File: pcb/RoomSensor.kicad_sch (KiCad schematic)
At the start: 38 parts, among them J1 FH34SRJ-24S-0.5SH50, J2 USB_C_Receptacle_PowerOnly_6P, J3 programming, Q1 SI1308EDL-T1-GE3, SW1 SW_Push, U1 ESP32-WROOM-32D

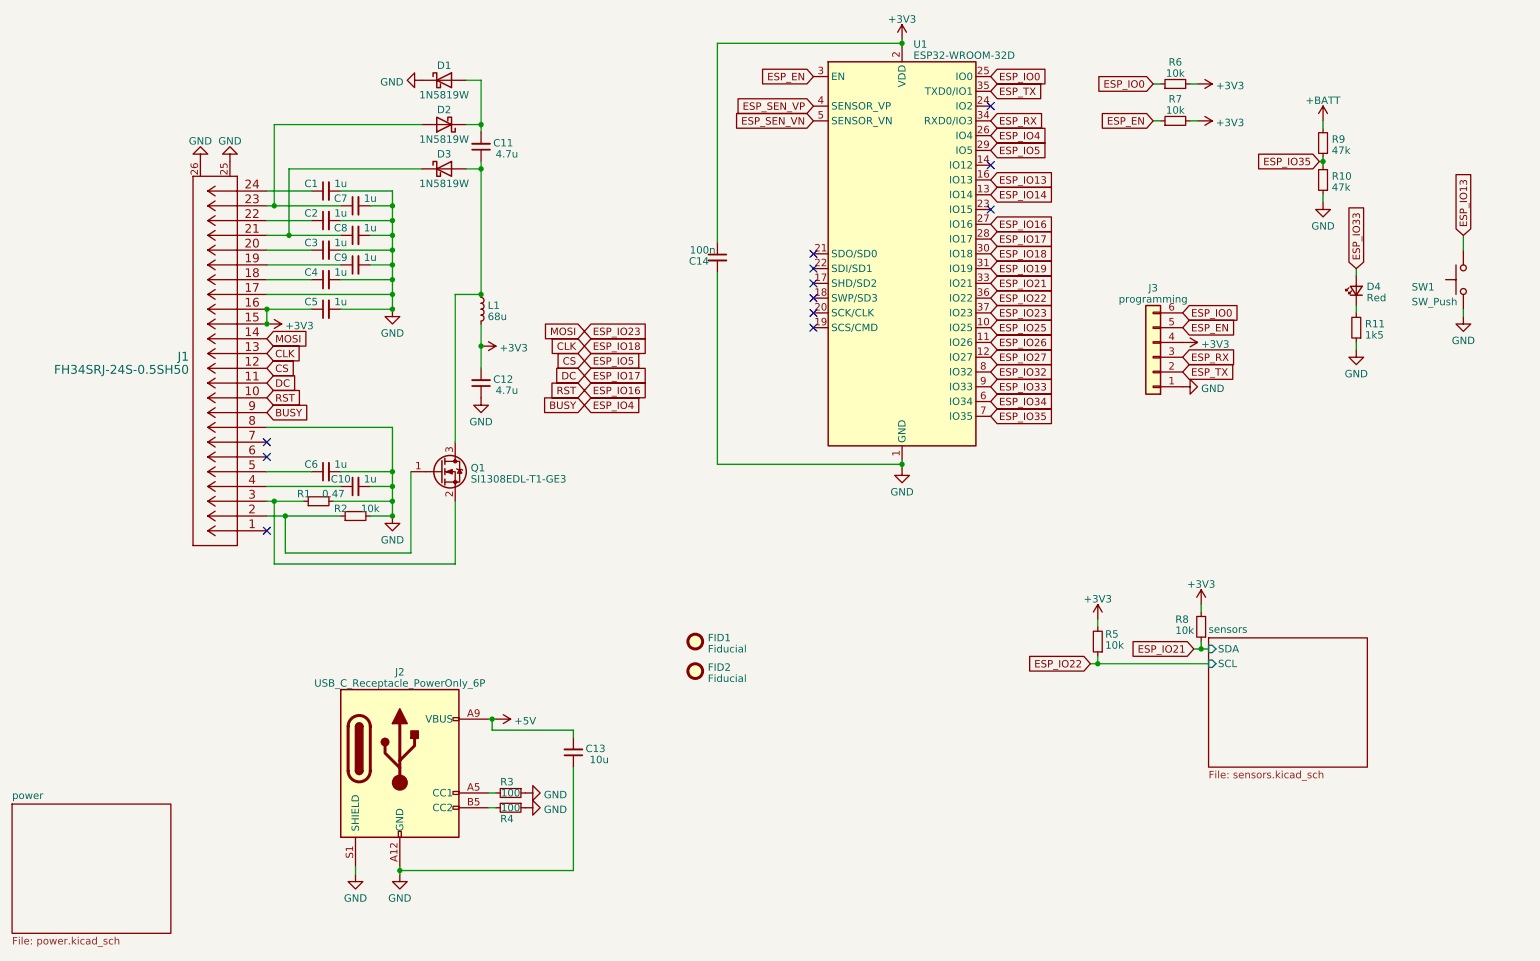
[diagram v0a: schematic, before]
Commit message: Increase PCB size and fix EPD pinout
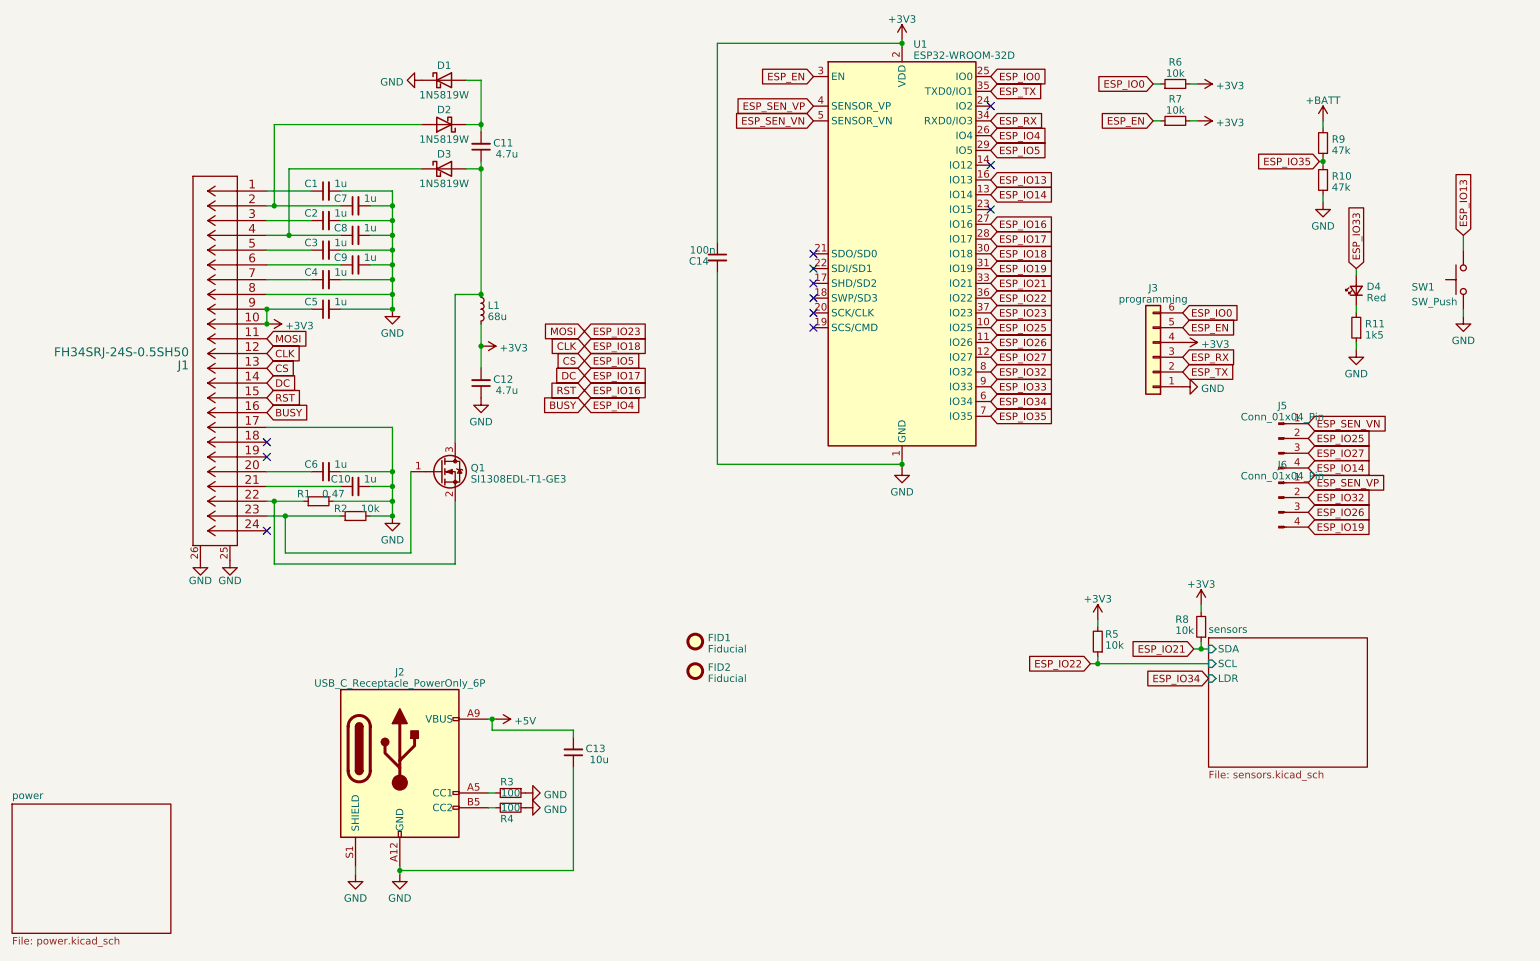
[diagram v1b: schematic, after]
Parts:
- added J5, J6: Conn_01x04_Pin, Connector_PinHeader_2.54mm:PinHeader_1x04_P2.54mm_Vertical, symbol Connector:Conn_01x04_Pin
- FID2: footprint Fiducial:Fiducial_0.5mm_Mask1mm -> Fiducial:Fiducial_0.5mm_Mask1.5mm
- J2: footprint Custom:TYPE-C-31-M-17_B -> Custom:TYPE-C 6P LCH10.0
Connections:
- net +3V3: now also J1.10, J1.9; no longer J1.15, J1.16
- net BUSY: now also J1.16; no longer J1.9
- net CLK: now also J1.12; no longer J1.13
- net CS: now also J1.13; no longer J1.12
- net DC: now also J1.14; no longer J1.11
- net ESP_IO14: now also J5.4 (Pin_4)
- net ESP_IO16: now also J1.15; no longer J1.10
- net ESP_IO19: now also J6.4 (Pin_4)
- net ESP_IO23: now also J1.11; no longer J1.14
- net ESP_IO25: now also J5.2 (Pin_2)
- net ESP_IO26: now also J6.3 (Pin_3)
- net ESP_IO27: now also J5.3 (Pin_3)
- net ESP_IO32: now also J6.2 (Pin_2)
- net ESP_SEN_VN: now also J5.1 (Pin_1)
- net ESP_SEN_VP: now also J6.1 (Pin_1)
- net at C4.1: now also J1.7; no longer J1.18
- net at C8.1, D3.1 (K): now also J1.4; no longer J1.21
- net at C3.1: now also J1.5; no longer J1.20
- net at Q1.2 (S), R1.1: now also J1.22; no longer J1.3
- net at Q1.1 (G), R2.1: now also J1.23; no longer J1.2
- net at C7.1, D2.2 (A): now also J1.2; no longer J1.23
- net at C2.1: now also J1.3; no longer J1.22
- net at J1.1: now also C1.1
- net at J1.19: no longer C9.1
- net at J1.24: no longer C1.1
- net at C10.1: now also J1.21; no longer J1.4
- net at C6.1: now also J1.20; no longer J1.5
- net at J1.6: now also C9.1
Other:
- sheet sensors ports: added LDR; removed none
- moved on the sheet: J1

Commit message: Fix low power issues
- Fix spurious EPD wakeups by adding pull-up to EPD reset line
- Reduce power consumption by switching sensors off with mosfet
- Connect button to reset to reduce power by not needing rtc gpio
- Add solder jumper for silent boot
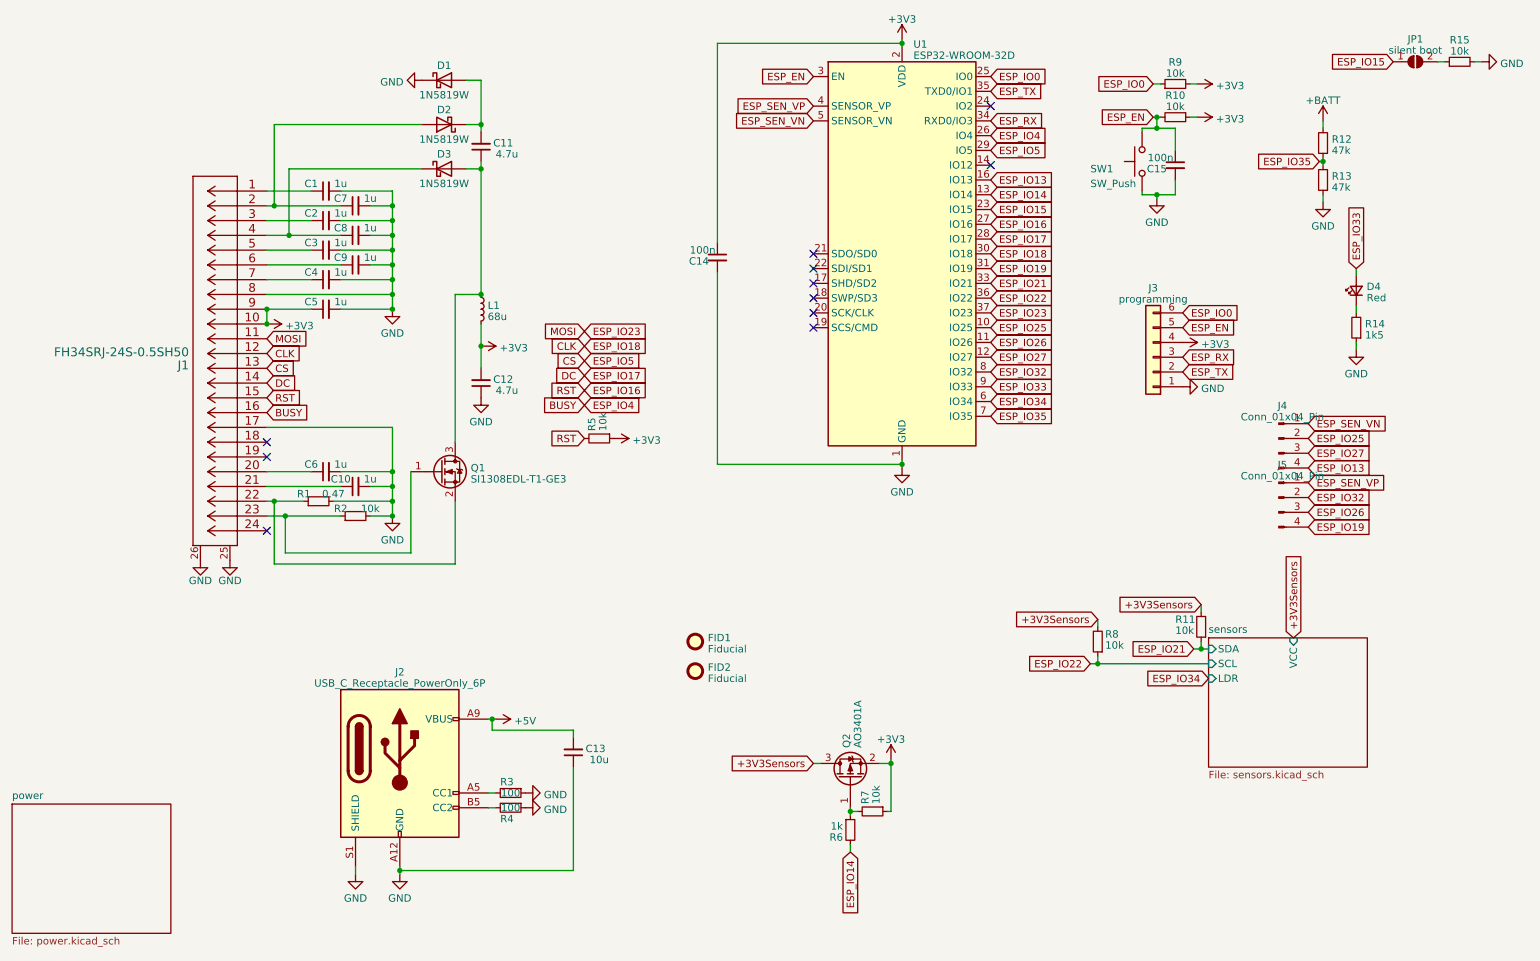
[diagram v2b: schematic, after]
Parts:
- added C15: 100n, Capacitor_SMD:C_0603_1608Metric, symbol Device:C_Small
- added JP1: silent boot, Jumper:SolderJumper-2_P1.3mm_Open_TrianglePad1.0x1.5mm, symbol Jumper:SolderJumper_2_Open
- added Q2: AO3401A, Package_TO_SOT_SMD:SOT-23, symbol Transistor_FET:AO3401A
- added R15, R5, R7: 10k, Resistor_SMD:R_0603_1608Metric, symbol Device:R_Small
- added R6: 1k, Resistor_SMD:R_0603_1608Metric, symbol Device:R_Small
- FID1: footprint Fiducial:Fiducial_0.5mm_Mask1mm -> Fiducial:Fiducial_0.5mm_Mask1.5mm
- renumbered J5 to J4, J6 to J5, R7 to R10, R8 to R11, R9 to R12, R10 to R13, R11 to R14, R5 to R8, R6 to R9
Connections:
- net +3V3: now also R10.1, Q2.2 (S), R5.1, R7.1; no longer R10.2, R11.2, R8.2
- net ESP_EN: now also R10.2, SW1.2, C15.1; no longer R10.1
- net ESP_IO13: now also J4.4 (Pin_4); no longer SW1.2
- net ESP_IO14: now also R6.2; no longer J4.4 (Pin_4)
- net ESP_IO16: now also R5.2
- net GND: now also C15.2, R15.2
- net ESP_IO15: now reaches U1.23 (IO15)
- net ESP_IO15: now also JP1.1 (A)
- new net: Q2.1 (G), R6.1, R7.2
- new net: JP1.2 (B), R15.1
- new net +3V3Sensors: Q2.3 (D), R11.2, R8.2
- no-connect marks 12 -> 11
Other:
- sheet sensors ports: added VCC; removed none
- moved on the sheet: R10, SW1

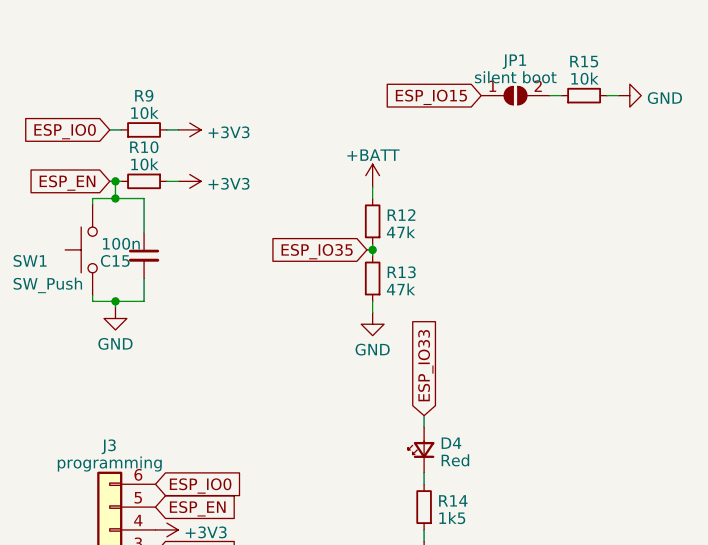
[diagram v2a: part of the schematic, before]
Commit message: Replace b- net with -Battery
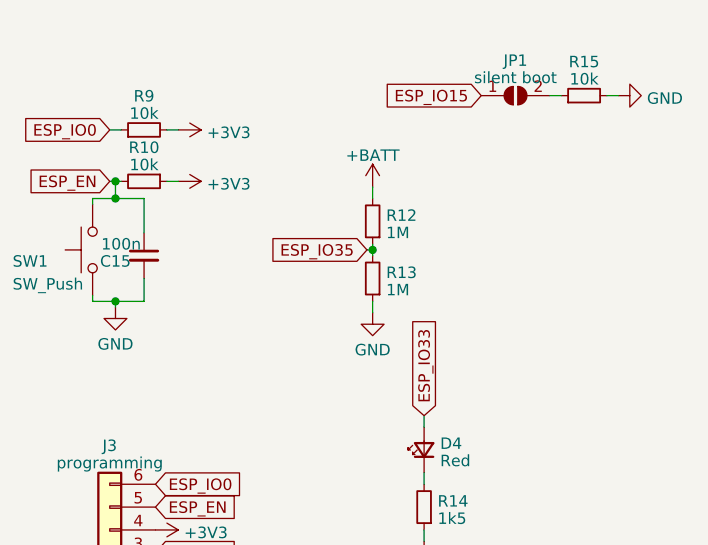
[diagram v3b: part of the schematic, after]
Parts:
- R12, R13: value 47k -> 1M
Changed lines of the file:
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@@
       (effects (font (size 1.27 1.27)) (justify right))
     )
-    (property "Value" "47k" (at 251.6886 38.7423 0)
+    (property "Value" "1M" (at 251.6886 38.7423 0)
       (effects (font (size 1.27 1.27)) (justify right))
     )
@@
       (effects (font (size 1.27 1.27)) (justify right))
     )
-    (property "Value" "47k" (at 251.6886 45.0923 0)
-      (effects (font (size 1.27 1.27)) (justify right))
-    )
+    (property "Value" "1M" (at 251.6886 45.0923 0)
+      (effects (font (size 1.27 1.27)) (justify right))
+    )
